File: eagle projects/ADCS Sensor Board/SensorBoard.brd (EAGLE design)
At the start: 91 x 91 mm, 85 parts, among them J5 HDR_10_EZFET_DEBUGGER, J6 MTI-1_8428-11B1-RK-TP, Q1 BC850SMD, Q2 IRF7507TRPBF, U1 MSP430F5529IPN, U2 LMV321, U3 ADS7841E_2K5, U4 LMV321, U5 LM20BIM7X_NOPB, U6 LMV321, Y1 32.768kHz, Y2 CSTCR4M00G15L99

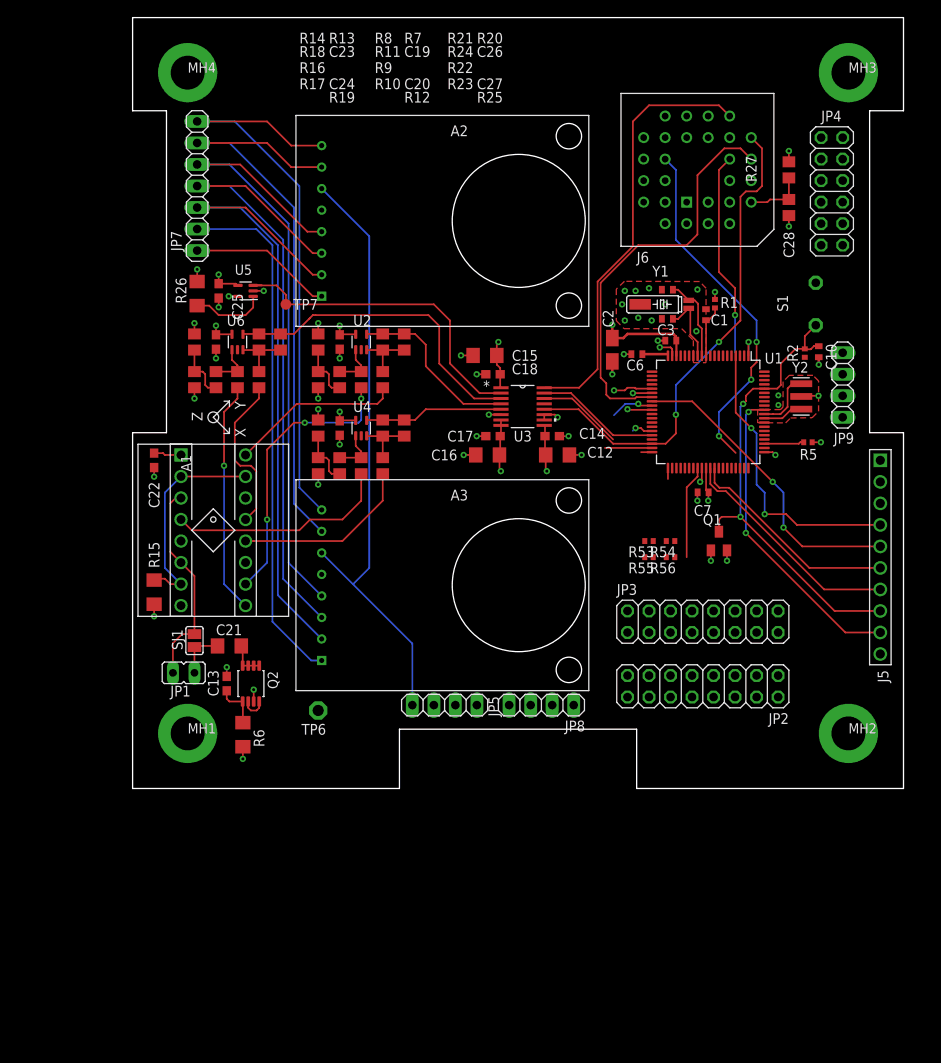
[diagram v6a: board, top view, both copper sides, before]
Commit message: Laid out pinout traces
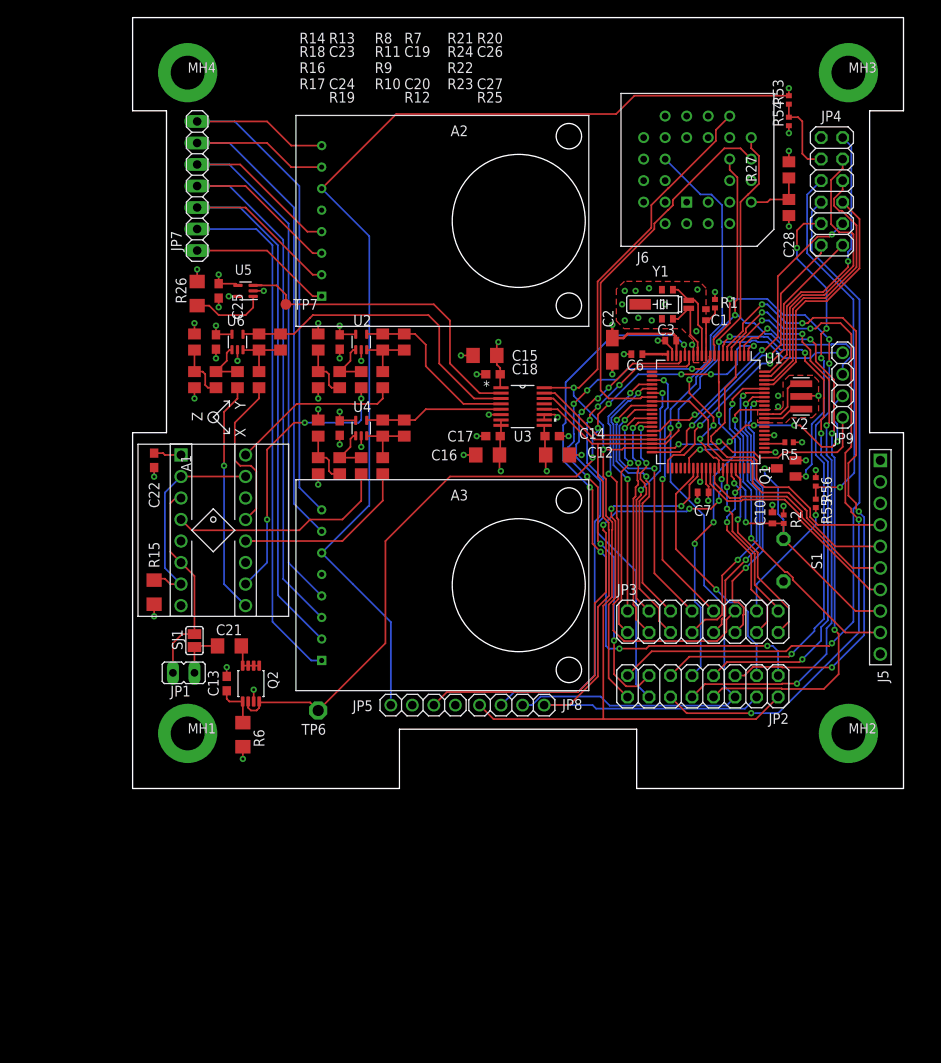
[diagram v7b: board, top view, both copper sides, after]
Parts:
- JP5, JP8, JP9: device pinhead:1X04 -> my_library:1X04
- moved R53 54.6 mm to (77.5, 81.3), turned to 90 degrees
- moved R54 51.5 mm to (77.5, 78.7), turned to 90 degrees
- moved S1 35.4 mm to (76.8, 24.4), turned to 90 degrees
- moved R55 20.7 mm to (80.6, 33.7), turned to 270 degrees
- moved C10 20.4 mm to (75.5, 31.9), turned to 90 degrees
- moved R2 19.8 mm to (76.9, 31.8), turned to 90 degrees
- moved R56 19.3 mm to (80.6, 36.2), turned to 270 degrees
- moved Q1 11.7 mm to (77.2, 37.8), turned to 90 degrees
- moved JP8 3.49 mm to (44.8, 9.84), turned to 0 degrees
- moved JP5 2.54 mm to (34.3, 9.84)
- moved R5 2.22 mm to (77.5, 40.9)
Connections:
- removed net P2.2: U1.31
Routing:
- net UCB0_SPI_MOSI: track 34.3 -> 133.4 mm, vias 1 -> 2
- net UCB0_SPI_CLK: track 56.5 -> 155.5 mm, vias 0 -> 4
- net HMC1053_RESET: track 5.63 -> 92.1 mm, vias 1 -> 6
- net ACT_BRD_3V_PRESENT: track 0.00 -> 81.9 mm, vias 0 -> 1
- net !CS!_SPEED_Z: track 0.00 -> 81.9 mm, vias 0 -> 4
- net UCB0_SPI_MISO: track 58.1 -> 135.0 mm
- net !CS!_CURRENT_SENSE_1: track 0.00 -> 76.4 mm, vias 0 -> 4
- net !CS!_SUN_Y-: track 0.00 -> 75.4 mm, vias 0 -> 5
- net !COUNT_EN: track 0.00 -> 75.0 mm, vias 0 -> 4
- net !CS!_SPEED_Y: track 0.00 -> 68.4 mm, vias 0 -> 4
- net !CS!_SPEED_X: track 0.00 -> 67.5 mm, vias 0 -> 4
- net !SPEED_CLR: track 0.00 -> 62.4 mm, vias 0 -> 4
- net !CS!_SUN_Z-: track 0.00 -> 60.1 mm, vias 0 -> 3
- net !CS!_CURRENT_SENSE_2: track 0.00 -> 58.5 mm, vias 0 -> 6
- net INIT_EPS_BURN_WIRE: track 0.00 -> 57.8 mm, vias 0 -> 4
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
